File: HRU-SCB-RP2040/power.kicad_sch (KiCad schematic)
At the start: 6 parts, among them J31 Conn_01x02_Pin, U4 NJM7805SDL1

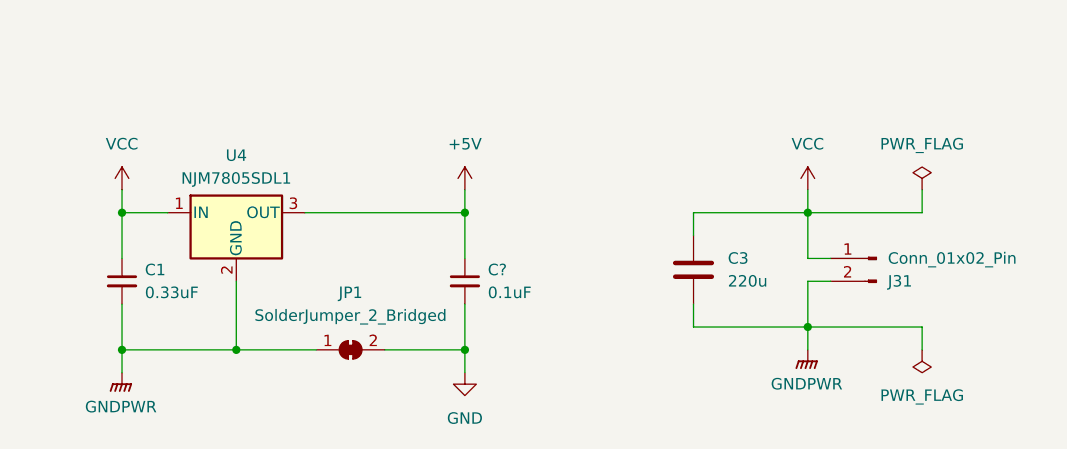
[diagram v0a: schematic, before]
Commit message: Delete PWM circuit
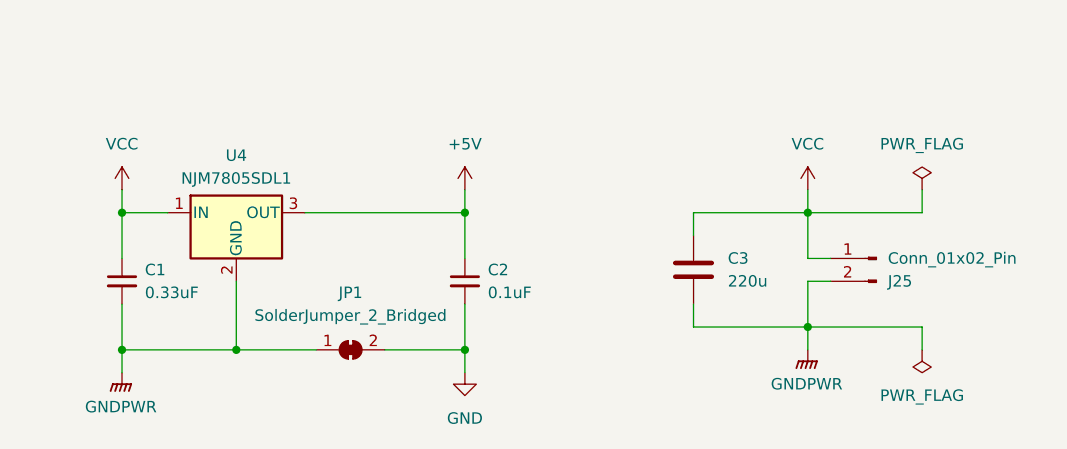
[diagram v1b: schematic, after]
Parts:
- gave numbers to parts that had none: 1
- renumbered J31 to J25
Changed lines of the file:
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@@
   (symbol (lib_id "power:GNDPWR") (at 50.8 68.58 0) (unit 1)
     (in_bom yes) (on_board yes) (dnp no) (fields_autoplaced)
-    (property "Reference" "#PWR026" (at 50.8 73.66 0)
+    (property "Reference" "#PWR022" (at 50.8 73.66 0)
       (effects (font (size 1.27 1.27)) hide)
     )
@@
       (project "HRU-SCB-RP2040"
         (path "/22d57d1f-fa00-4148-a62a-8eb596ebbd21/8865bb96-b424-4214-9ee7-9e2e6881a969"
-          (reference "#PWR026") (unit 1)
+          (reference "#PWR022") (unit 1)
         )
       )
@@
   (symbol (lib_id "power:+5V") (at 88.9 48.26 0) (unit 1)
     (in_bom yes) (on_board yes) (dnp no) (fields_autoplaced)
-    (property "Reference" "#PWR027" (at 88.9 52.07 0)
+    (property "Reference" "#PWR023" (at 88.9 52.07 0)
       (effects (font (size 1.27 1.27)) hide)
     )
@@
       (project "HRU-SCB-RP2040"
         (path "/22d57d1f-fa00-4148-a62a-8eb596ebbd21/8865bb96-b424-4214-9ee7-9e2e6881a969"
-          (reference "#PWR027") (unit 1)
+          (reference "#PWR023") (unit 1)
         )
       )
@@
   (symbol (lib_id "power:VCC") (at 50.8 48.26 0) (unit 1)
     (in_bom yes) (on_board yes) (dnp no) (fields_autoplaced)
-    (property "Reference" "#PWR025" (at 50.8 52.07 0)
+    (property "Reference" "#PWR021" (at 50.8 52.07 0)
       (effects (font (size 1.27 1.27)) hide)
     )
@@
       (project "HRU-SCB-RP2040"
         (path "/22d57d1f-fa00-4148-a62a-8eb596ebbd21/8865bb96-b424-4214-9ee7-9e2e6881a969"
-          (reference "#PWR025") (unit 1)
+          (reference "#PWR021") (unit 1)
         )
       )
@@
   (symbol (lib_id "Connector:Conn_01x02_Pin") (at 134.62 55.88 0) (mirror y) (unit 1)
     (in_bom yes) (on_board yes) (dnp no)
-    (property "Reference" "J31" (at 135.89 58.42 0)
+    (property "Reference" "J25" (at 135.89 58.42 0)
       (effects (font (size 1.27 1.27)) (justify right))
     )
@@
       (project "HRU-SCB-RP2040"
         (path "/22d57d1f-fa00-4148-a62a-8eb596ebbd21/8865bb96-b424-4214-9ee7-9e2e6881a969"
-          (reference "J31") (unit 1)
+          (reference "J25") (unit 1)
         )
       )
@@
   (symbol (lib_id "power:PWR_FLAG") (at 139.7 66.04 180) (unit 1)
     (in_bom yes) (on_board yes) (dnp no) (fields_autoplaced)
-    (property "Reference" "#FLG04" (at 139.7 67.945 0)
+    (property "Reference" "#FLG02" (at 139.7 67.945 0)
       (effects (font (size 1.27 1.27)) hide)
     )
@@
       (project "HRU-SCB-RP2040"
         (path "/22d57d1f-fa00-4148-a62a-8eb596ebbd21/8865bb96-b424-4214-9ee7-9e2e6881a969"
-          (reference "#FLG04") (unit 1)
+          (reference "#FLG02") (unit 1)
         )
       )
@@
   (symbol (lib_id "power:GNDPWR") (at 127 66.04 0) (unit 1)
     (in_bom yes) (on_board yes) (dnp no) (fields_autoplaced)
-    (property "Reference" "#PWR030" (at 127 71.12 0)
+    (property "Reference" "#PWR026" (at 127 71.12 0)
       (effects (font (size 1.27 1.27)) hide)
     )
@@
       (project "HRU-SCB-RP2040"
         (path "/22d57d1f-fa00-4148-a62a-8eb596ebbd21/8865bb96-b424-4214-9ee7-9e2e6881a969"
-          (reference "#PWR030") (unit 1)
+          (reference "#PWR026") (unit 1)
         )
       )
@@
   (symbol (lib_id "Device:C_Small") (at 88.9 58.42 0) (unit 1)
     (in_bom yes) (on_board yes) (dnp no) (fields_autoplaced)
-    (property "Reference" "C?" (at 91.44 57.1563 0)
+    (property "Reference" "C2" (at 91.44 57.1563 0)
       (effects (font (size 1.27 1.27)) (justify left))
     )
@@
     (instances
       (project "HRU-SCB-RP2040"
-        (path "/22d57d1f-fa00-4148-a62a-8eb596ebbd21/e77e8245-6b3f-4da7-90e6-d027ac806a87"
-          (reference "C?") (unit 1)
-        )
         (path "/22d57d1f-fa00-4148-a62a-8eb596ebbd21/8865bb96-b424-4214-9ee7-9e2e6881a969"
           (reference "C2") (unit 1)
@@
   (symbol (lib_id "power:GND") (at 88.9 68.58 0) (unit 1)
     (in_bom yes) (on_board yes) (dnp no) (fields_autoplaced)
-    (property "Reference" "#PWR028" (at 88.9 74.93 0)
+    (property "Reference" "#PWR024" (at 88.9 74.93 0)
       (effects (font (size 1.27 1.27)) hide)
     )
@@
       (project "HRU-SCB-RP2040"
         (path "/22d57d1f-fa00-4148-a62a-8eb596ebbd21/8865bb96-b424-4214-9ee7-9e2e6881a969"
-          (reference "#PWR028") (unit 1)
+          (reference "#PWR024") (unit 1)
         )
       )
@@
   (symbol (lib_id "power:VCC") (at 127 48.26 0) (unit 1)
     (in_bom yes) (on_board yes) (dnp no) (fields_autoplaced)
-    (property "Reference" "#PWR029" (at 127 52.07 0)
+    (property "Reference" "#PWR025" (at 127 52.07 0)
       (effects (font (size 1.27 1.27)) hide)
     )
@@
       (project "HRU-SCB-RP2040"
         (path "/22d57d1f-fa00-4148-a62a-8eb596ebbd21/8865bb96-b424-4214-9ee7-9e2e6881a969"
-          (reference "#PWR029") (unit 1)
-        )
-      )
+          (reference "#PWR025") (unit 1)
+        )
+      )

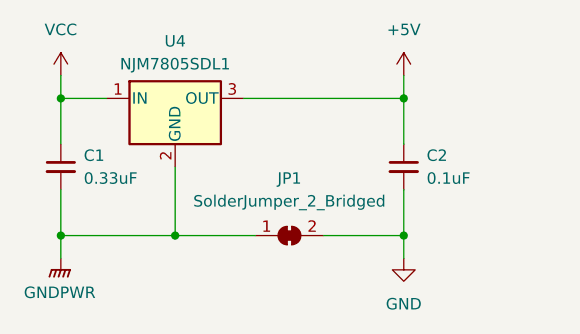
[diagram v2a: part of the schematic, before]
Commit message: Update DCDC for DIP soldering
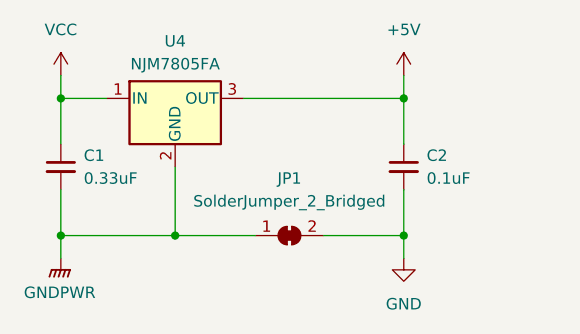
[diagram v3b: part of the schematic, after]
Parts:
- U4: value NJM7805SDL1 -> NJM7805FA; footprint Package_TO_SOT_SMD:TO-252-2 -> Package_TO_SOT_THT:TO-220F-3_Horizontal_TabDown
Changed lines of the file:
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@@
 			)
 		)
-		(property "Value" "NJM7805SDL1"
+		(property "Value" "NJM7805FA"
 			(at 63.5 46.99 0)
 			(effects
@@
 			)
 		)
-		(property "Footprint" "Package_TO_SOT_SMD:TO-252-2"
+		(property "Footprint" "Package_TO_SOT_THT:TO-220F-3_Horizontal_TabDown"
 			(at 64.135 54.61 0)
 			(effects

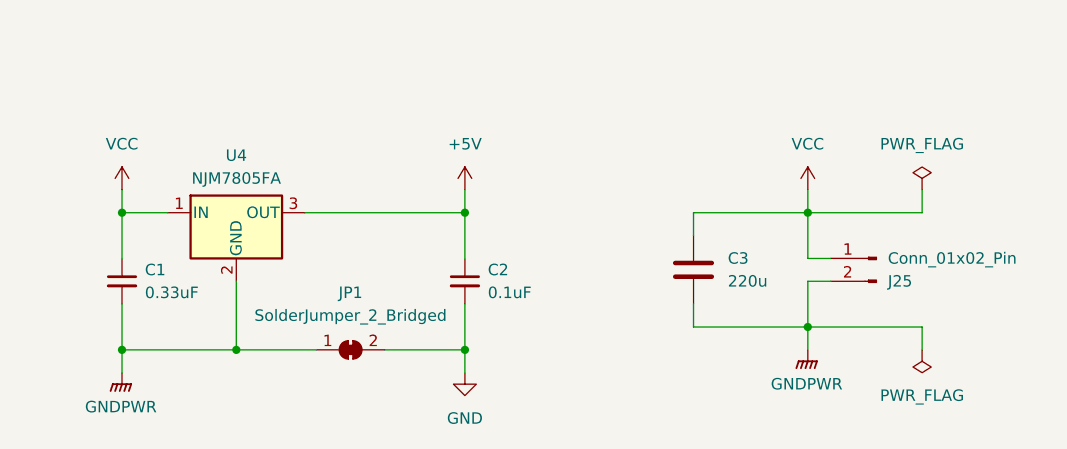
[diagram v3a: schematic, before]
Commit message: Modify footprint of the registers and regulators
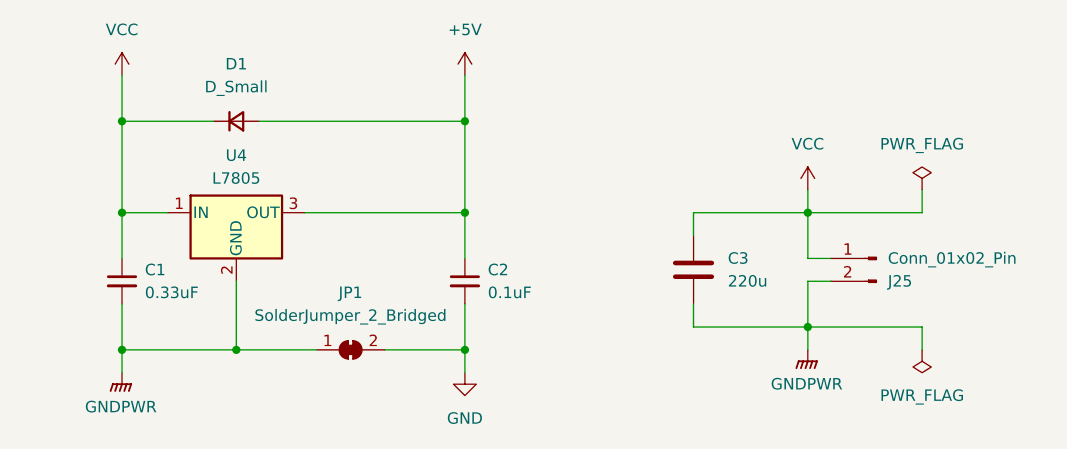
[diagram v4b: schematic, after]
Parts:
- added D1: D_Small, Diode_THT:D_T-1_P12.70mm_Horizontal, symbol Device:D_Small
- U4: value NJM7805FA -> L7805
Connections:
- net +5V: now also D1.2 (A)
- net VCC: now also D1.1 (K)
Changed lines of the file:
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@@
+	)
+	(junction
+		(at 88.9 40.64)
+		(diameter 0)
+		(color 0 0 0 0)
 	)
 	(junction
@@
 	)
 	(junction
+		(at 50.8 40.64)
+		(diameter 0)
+		(color 0 0 0 0)
+	)
+	(junction
 		(at 63.5 66.04)
 		(diameter 0)
@@
 	(wire
 		(pts
-			(xy 50.8 48.26) (xy 50.8 50.8)
-		)
-		(stroke
-			(width 0)
-			(type default)
-		)
-	)
-	(wire
-		(pts
-			(xy 88.9 48.26) (xy 88.9 50.8)
+			(xy 50.8 35.56) (xy 50.8 40.64)
+		)
+		(stroke
+			(width 0)
+			(type default)
+		)
+	)
+	(wire
+		(pts
+			(xy 88.9 35.56) (xy 88.9 40.64)
 		)
 		(stroke
@@
 	(wire
 		(pts
+			(xy 50.8 40.64) (xy 50.8 50.8)
+		)
+		(stroke
+			(width 0)
+			(type default)
+		)
+	)
+	(wire
+		(pts
+			(xy 88.9 40.64) (xy 88.9 50.8)
+		)
+		(stroke
+			(width 0)
+			(type default)
+		)
+	)
+	(wire
+		(pts
 			(xy 114.3 63.5) (xy 114.3 60.96)
 		)
@@
 	(wire
 		(pts
+			(xy 50.8 40.64) (xy 60.96 40.64)
+		)
+		(stroke
+			(width 0)
+			(type default)
+		)
+	)
+	(wire
+		(pts
 			(xy 139.7 63.5) (xy 127 63.5)
 		)
@@
 		(pts
 			(xy 127 48.26) (xy 127 50.8)
+		)
+		(stroke
+			(width 0)
+			(type default)
+		)
+	)
+	(wire
+		(pts
+			(xy 66.04 40.64) (xy 88.9 40.64)
 		)
 		(stroke
@@
 	(symbol
 		(lib_id "power:+5V")
-		(at 88.9 48.26 0)
+		(at 88.9 35.56 0)
 		(unit 1)
 		(exclude_from_sim no)
@@
 		(fields_autoplaced yes)
 		(property "Reference" "#PWR023"
-			(at 88.9 52.07 0)
+			(at 88.9 39.37 0)
 			(effects
 				(font
@@
 		)
 		(property "Value" "+5V"
-			(at 88.9 43.18 0)
+			(at 88.9 30.48 0)
 			(effects
 				(font
@@
 		)
 		(property "Footprint" ""
-			(at 88.9 48.26 0)
+			(at 88.9 35.56 0)
 			(effects
 				(font
@@
 		)
 		(property "Datasheet" ""
-			(at 88.9 48.26 0)
+			(at 88.9 35.56 0)
 			(effects
 				(font
@@
 		)
 		(property "Description" ""
-			(at 88.9 48.26 0)
+			(at 88.9 35.56 0)
 			(effects
 				(font
@@
 	(symbol
 		(lib_id "power:VCC")
-		(at 50.8 48.26 0)
+		(at 50.8 35.56 0)
 		(unit 1)
 		(exclude_from_sim no)
@@
 		(fields_autoplaced yes)
 		(property "Reference" "#PWR021"
-			(at 50.8 52.07 0)
+			(at 50.8 39.37 0)
 			(effects
 				(font
@@
 		)
 		(property "Value" "VCC"
-			(at 50.8 43.18 0)
+			(at 50.8 30.48 0)
 			(effects
 				(font
@@
 		)
 		(property "Footprint" ""
-			(at 50.8 48.26 0)
+			(at 50.8 35.56 0)
 			(effects
 				(font
@@
 		)
 		(property "Datasheet" ""
-			(at 50.8 48.26 0)
+			(at 50.8 35.56 0)
 			(effects
 				(font
@@
 		)
 		(property "Description" ""
-			(at 50.8 48.26 0)
+			(at 50.8 35.56 0)
 			(effects
 				(font
@@
 			)
 		)
-		(property "Value" "NJM7805FA"
+		(property "Value" "L7805"
 			(at 63.5 46.99 0)
 			(effects
@@
 					(unit 1)
 				)
+			)
+		)
+	)
+	(symbol
+		(lib_id "Device:D_Small")
+		(at 63.5 40.64 0)
+		(unit 1)
+		(exclude_from_sim no)
+		(in_bom yes)
+		(on_board yes)
+		(dnp no)
+		(fields_autoplaced yes)
+		(property "Reference" "D1"
+			(at 63.5 34.29 0)
+			(effects
+				(font
+					(size 1.27 1.27)
+				)
+			)
+		)
+		(property "Value" "D_Small"
+			(at 63.5 36.83 0)
+			(effects
+				(font
+					(size 1.27 1.27)
+				)
+			)
+		)
+		(property "Footprint" "Diode_THT:D_T-1_P12.70mm_Horizontal"
+			(at 63.5 40.64 90)
+			(effects
+				(font
+					(size 1.27 1.27)
+				)
+				(hide yes)
+			)
+		)
+		(property "Datasheet" "~"
+			(at 63.5 40.64 90)
+			(effects
+				(font
+					(size 1.27 1.27)
+				)
+				(hide yes)
+			)
+		)
+		(property "Description" "Diode, small symbol"
+			(at 63.5 40.64 0)
+			(effects
+				(font
+					(size 1.27 1.27)
+				)
+				(hide yes)
+			)
+		)
+		(property "Sim.Device" "D"
+			(at 63.5 40.64 0)
+			(effects
+				(font
+					(size 1.27 1.27)
+				)
+				(hide yes)
+			)
+		)
+		(property "Sim.Pins" "1=K 2=A"
+			(at 63.5 40.64 0)
+			(effects
+				(font
+					(size 1.27 1.27)
+				)
+				(hide yes)
+			)
+		)
+		(pin "1"
+		)
+		(pin "2"
+		)
+		(instances
+			(project ""
+				(path "/22d57d1f-fa00-4148-a62a-8eb596ebbd21/8865bb96-b424-4214-9ee7-9e2e6881a969"
+					(reference "D1")
+					(unit 1)
+				)

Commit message: update: circuit design of HRU-SCB-RP2040
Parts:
- removed D1: D_Small, Diode_THT:D_T-1_P12.70mm_Horizontal, symbol Device:D_Small
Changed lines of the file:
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@@
 (kicad_sch
-	(version 20231120)
+	(version 20250114)
 	(generator "eeschema")
-	(generator_version "8.0")
+	(generator_version "9.0")
 	(paper "A4")
 	(junction
@@
 	)
 	(junction
-		(at 88.9 40.64)
-		(diameter 0)
-		(color 0 0 0 0)
-	)
-	(junction
 		(at 50.8 66.04)
 		(diameter 0)
@@
 	)
 	(junction
-		(at 50.8 40.64)
-		(diameter 0)
-		(color 0 0 0 0)
-	)
-	(junction
 		(at 63.5 66.04)
 		(diameter 0)
@@
 	(wire
 		(pts
-			(xy 50.8 35.56) (xy 50.8 40.64)
-		)
-		(stroke
-			(width 0)
-			(type default)
-		)
-	)
-	(wire
-		(pts
-			(xy 88.9 35.56) (xy 88.9 40.64)
+			(xy 88.9 35.56) (xy 88.9 50.8)
 		)
 		(stroke
@@
 	(wire
 		(pts
-			(xy 50.8 40.64) (xy 50.8 50.8)
-		)
-		(stroke
-			(width 0)
-			(type default)
-		)
-	)
-	(wire
-		(pts
-			(xy 88.9 40.64) (xy 88.9 50.8)
+			(xy 50.8 35.56) (xy 50.8 50.8)
 		)
 		(stroke
@@
 	(wire
 		(pts
-			(xy 50.8 40.64) (xy 60.96 40.64)
-		)
-		(stroke
-			(width 0)
-			(type default)
-		)
-	)
-	(wire
-		(pts
 			(xy 139.7 63.5) (xy 127 63.5)
 		)
@@
 		(pts
 			(xy 127 48.26) (xy 127 50.8)
-		)
-		(stroke
-			(width 0)
-			(type default)
-		)
-	)
-	(wire
-		(pts
-			(xy 66.04 40.64) (xy 88.9 40.64)
 		)
 		(stroke
@@
 					(unit 1)
 				)
-			)
-		)
-	)
-	(symbol
-		(lib_id "Device:D_Small")
-		(at 63.5 40.64 0)
-		(unit 1)
-		(exclude_from_sim no)
-		(in_bom yes)
-		(on_board yes)
-		(dnp no)
-		(fields_autoplaced yes)
-		(property "Reference" "D1"
-			(at 63.5 34.29 0)
-			(effects
-				(font
-					(size 1.27 1.27)
-				)
-			)
-		)
-		(property "Value" "D_Small"
-			(at 63.5 36.83 0)
-			(effects
-				(font
-					(size 1.27 1.27)
-				)
-			)
-		)
-		(property "Footprint" "Diode_THT:D_T-1_P12.70mm_Horizontal"
-			(at 63.5 40.64 90)
-			(effects
-				(font
-					(size 1.27 1.27)
-				)
-				(hide yes)
-			)
-		)
-		(property "Datasheet" "~"
-			(at 63.5 40.64 90)
-			(effects
-				(font
-					(size 1.27 1.27)
-				)
-				(hide yes)
-			)
-		)
-		(property "Description" "Diode, small symbol"
-			(at 63.5 40.64 0)
-			(effects
-				(font
-					(size 1.27 1.27)
-				)
-				(hide yes)
-			)
-		)
-		(property "Sim.Device" "D"
-			(at 63.5 40.64 0)
-			(effects
-				(font
-					(size 1.27 1.27)
-				)
-				(hide yes)
-			)
-		)
-		(property "Sim.Pins" "1=K 2=A"
-			(at 63.5 40.64 0)
-			(effects
-				(font
-					(size 1.27 1.27)
-				)
-				(hide yes)
-			)
-		)
-		(pin "1"
-		)
-		(pin "2"
-		)
-		(instances
-			(project ""
-				(path "/22d57d1f-fa00-4148-a62a-8eb596ebbd21/8865bb96-b424-4214-9ee7-9e2e6881a969"
-					(reference "D1")
-					(unit 1)
-				)

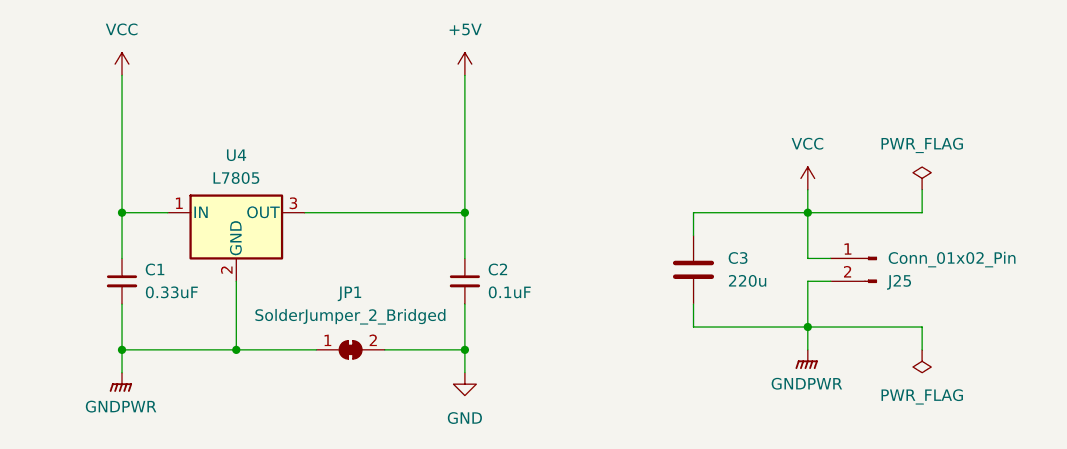
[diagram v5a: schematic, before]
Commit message: Update: apply super DCDC
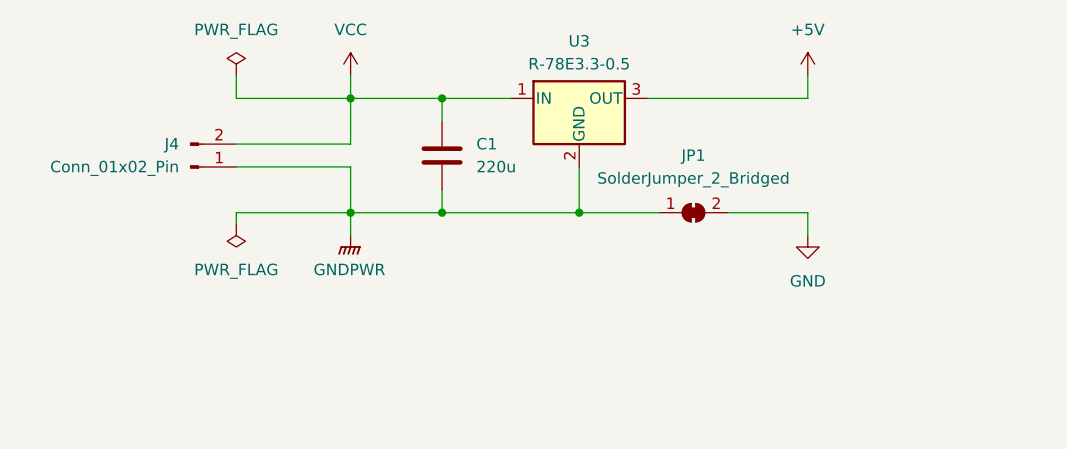
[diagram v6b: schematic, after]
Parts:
- removed C1: 0.33uF, Capacitor_THT:C_Disc_D3.8mm_W2.6mm_P2.50mm, symbol Device:C_Small
- removed C2: 0.1uF, Capacitor_THT:C_Disc_D3.8mm_W2.6mm_P2.50mm, symbol Device:C_Small
- removed U4: L7805, Package_TO_SOT_THT:TO-220F-3_Horizontal_TabDown, symbol Regulator_Linear:L7805
- added U3: R-78E3.3-0.5, Converter_DCDC:Converter_DCDC_RECOM_R-78E-0.5_THT, symbol Converter_DCDC:R-78E3.3-0.5
- J4: renamed from J25; footprint Connector_JST:JST_VH_B2P-VH_1x02_P3.96mm_Vertical -> Connector_AMASS:AMASS_XT30UPB-M_1x02_P5.0mm_Vertical
- renumbered C3 to C1
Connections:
- net +5V: now also U3.3 (OUT)
- net GNDPWR: now also J4.1 (Pin_1), U3.2 (GND); no longer J4.2 (Pin_2)
- net VCC: now also J4.2 (Pin_2), U3.1 (IN); no longer J4.1 (Pin_1)
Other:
- moved on the sheet: C1, J4, JP1
